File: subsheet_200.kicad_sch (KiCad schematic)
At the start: 13 parts, among them J200 DIN-5S — MIDI OUT/THRU, J201 DIN-5S — MIDI IN, U200 MC6850_PHY, U208 PC900_PHY, U210 7406_PHY

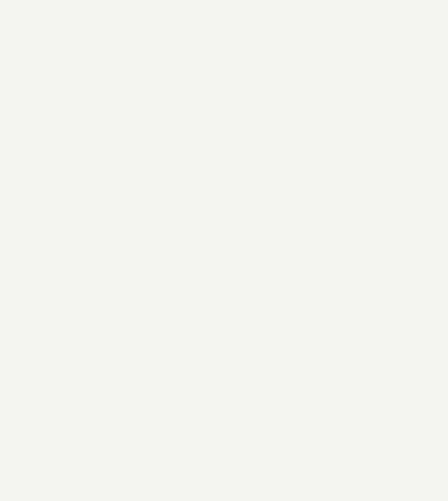
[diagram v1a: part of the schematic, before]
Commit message: add gnd/vcc symbol to start replacing local labels
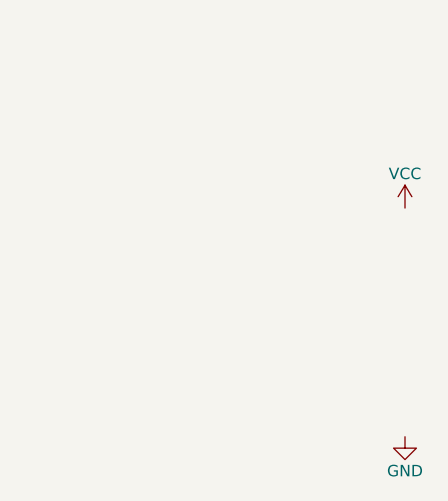
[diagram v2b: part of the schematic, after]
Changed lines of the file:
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@@
     (pin "8")
   )
+  (symbol (lib_id "power:GND") (at 185.42 233.68 0) (unit 1)
+    (in_bom yes) (on_board yes)
+    (property "Reference" "#PWR?" (id 0) (at 185.42 240.03 0)
+      (effects (font (size 1.27 1.27)) hide)
+    )
+    (property "Value" "GND" (id 1) (at 185.42 237.49 0))
+    (property "Footprint" "" (id 2) (at 185.42 233.68 0)
+      (effects (font (size 1.27 1.27)) hide)
+    )
+    (property "Datasheet" "" (id 3) (at 185.42 233.68 0)
+      (effects (font (size 1.27 1.27)) hide)
+    )
+    (pin "1")
+  )
+  (symbol (lib_id "power:VCC") (at 185.42 208.28 0) (unit 1)
+    (in_bom yes) (on_board yes)
+    (property "Reference" "#PWR?" (id 0) (at 185.42 212.09 0)
+      (effects (font (size 1.27 1.27)) hide)
+    )
+    (property "Value" "VCC" (id 1) (at 185.42 204.47 0))
+    (property "Footprint" "" (id 2) (at 185.42 208.28 0)
+      (effects (font (size 1.27 1.27)) hide)
+    )
+    (property "Datasheet" "" (id 3) (at 185.42 208.28 0)
+      (effects (font (size 1.27 1.27)) hide)
+    )
+    (pin "1")
+  )
 )
